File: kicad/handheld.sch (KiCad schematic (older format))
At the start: 23 parts, among them J1 Conn_01x08, J2 61300311121, J3 AVR-PDI-6, SW1 HOLD, SW2 PAUSE, SW3 SDROP, SW4 HDROP, SW5 ROTR, SW6 RIGHT, SW7 ROTL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

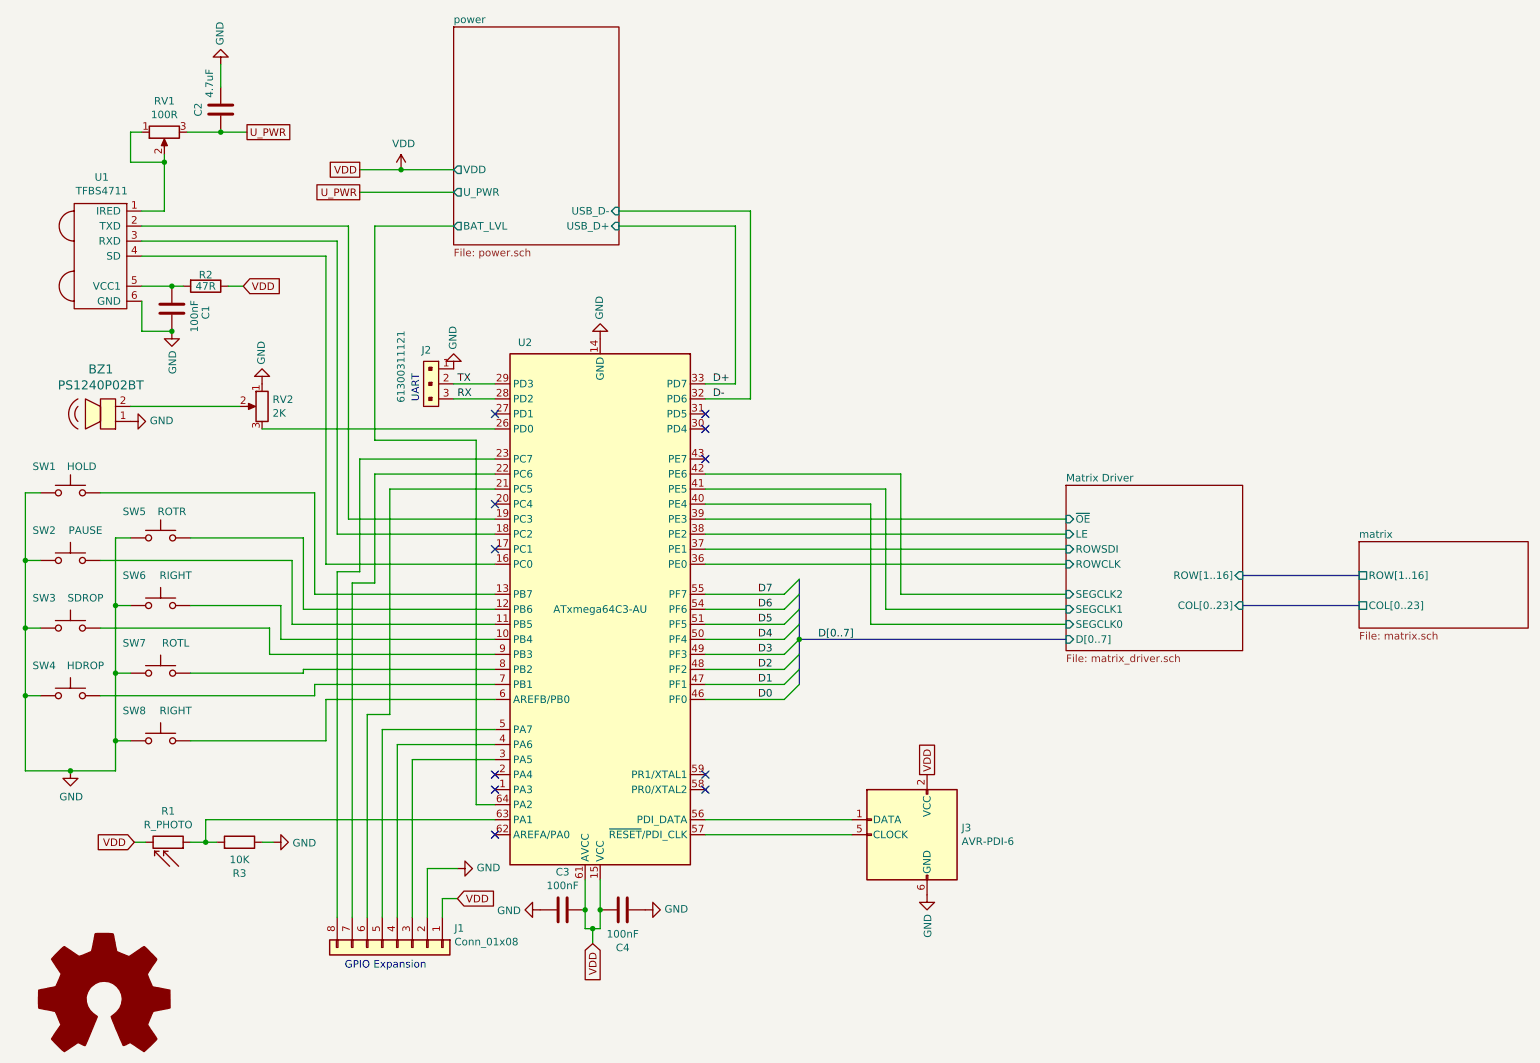
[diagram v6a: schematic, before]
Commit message: Added power plane and reassigned pinout
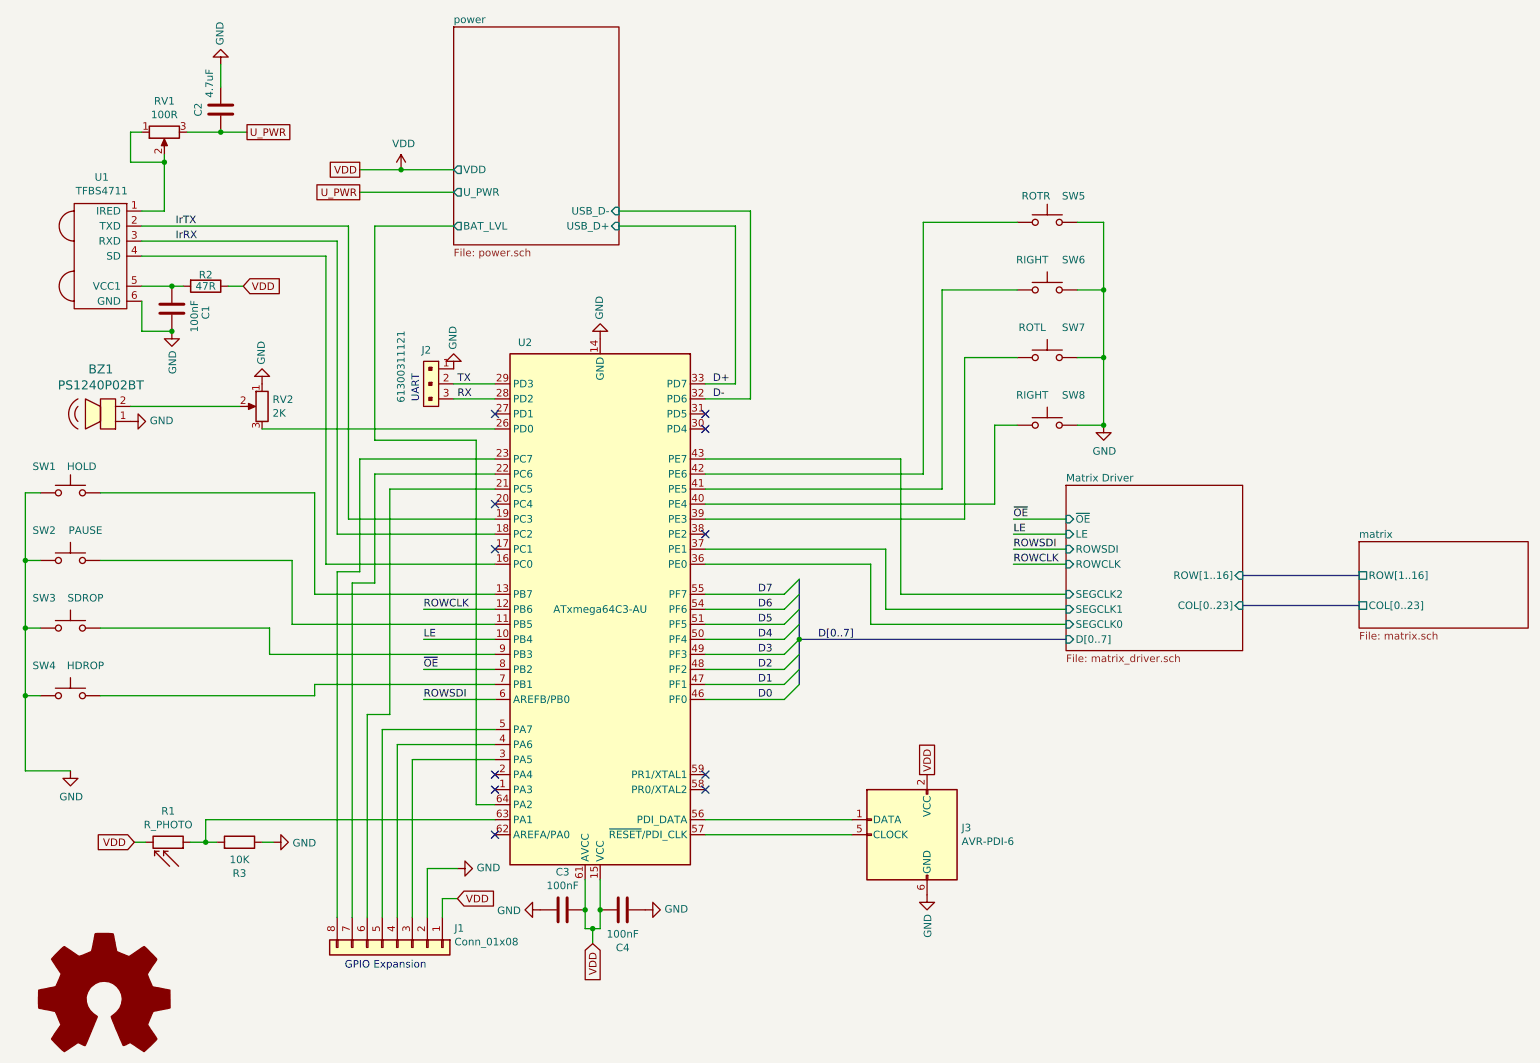
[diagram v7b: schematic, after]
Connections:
- net Matrix Driver/ROWCLK is gone; now on net Matrix Driver/SEGCLK0: U2.36 (PE0)
- net Matrix Driver/ROWSDI is gone; now on net Matrix Driver/SEGCLK1: U2.37 (PE1)
- net Matrix Driver/~OE is gone; now on an unnamed net: U2.39 (PE3)
- net Matrix Driver/SEGCLK0: no longer U2.40 (PE4)
- net Matrix Driver/SEGCLK1: no longer U2.41 (PE5)
- net Matrix Driver/SEGCLK2: now also U2.43 (PE7); no longer U2.42 (PE6)
- net at SW8.2: now also U2.40 (PE4); no longer U2.6 (AREFB/PB0)
- net at SW7.2: no longer U2.8 (PB2)
- net at SW6.2: now also U2.41 (PE5); no longer U2.10 (PB4)
- net at SW5.2: now also U2.42 (PE6); no longer U2.12 (PB6)
- net IrRX: now reaches U1.3 (RXD), U2.18 (PC2)
- net IrTX: now reaches U1.2 (TXD), U2.19 (PC3)
- net Matrix Driver/LE: no longer names the net of U2.38 (PE2)
- new net LE: U2.10 (PB4)
- new net ROWCLK: U2.12 (PB6)
- new net ROWSDI: U2.6 (AREFB/PB0)
- new net ~OE: U2.8 (PB2)
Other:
- moved on the sheet: SW5, SW6, SW7, SW8
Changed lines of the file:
@@
 TX
 Wire Wire Line
-	7550 4375 5150 4375
-Wire Wire Line
-	5150 4275 7550 4275
-Wire Wire Line
-	7550 4175 5150 4175
-Wire Wire Line
-	5150 4075 7550 4075
-Wire Wire Line
 	7550 4775 6250 4775
 Wire Wire Line
-	6250 4775 6250 3975
-Wire Wire Line
-	6250 3975 5150 3975
-Wire Wire Line
 	7550 4675 6350 4675
 Wire Wire Line
-	6350 4675 6350 3875
-Wire Wire Line
-	6350 3875 5150 3875
-Wire Wire Line
 	7550 4575 6450 4575
-Wire Wire Line
-	6450 4575 6450 3775
-Wire Wire Line
-	6450 3775 5150 3775
 $Comp
 L local:TFBS4711 U1
@@
 NoConn ~ 5150 3375
 NoConn ~ 5150 3475
-NoConn ~ 5150 3675
 NoConn ~ 3750 3975
 NoConn ~ 3750 4275
@@
 	1    0    0    -1
 $EndComp
-Connection ~ 925  5750
-Wire Wire Line
-	925  5750 1225 5750
-Wire Wire Line
-	1325 5550 1225 5550
-Connection ~ 1225 5550
-Wire Wire Line
-	1225 5550 1225 5750
-Wire Wire Line
-	2625 5550 2625 5275
-Wire Wire Line
-	2625 5275 3750 5275
-Wire Wire Line
-	2625 5550 1725 5550
+Wire Wire Line
+	3275 5275 3750 5275
 Wire Wire Line
 	2550 5250 2550 5175
@@
 	2550 5175 3750 5175
 Wire Wire Line
-	2475 5100 2475 5075
-Wire Wire Line
-	2475 5075 3750 5075
+	3275 5075 3750 5075
 Wire Wire Line
 	2250 4800 2250 4975
@@
 	2550 4575 3750 4575
 Wire Wire Line
-	2475 4200 2475 4675
-Wire Wire Line
-	2475 4675 3750 4675
+	3275 4675 3750 4675
 Wire Wire Line
 	2400 4350 2400 4775
@@
 	2400 4775 3750 4775
 Wire Wire Line
-	2325 4650 2325 4875
-Wire Wire Line
-	2325 4875 3750 4875
+	3275 4875 3750 4875
 $Comp
 L Switch:SW_Push SW4
@@
 Wire Wire Line
 	625  3900 625  4350
-Wire Wire Line
-	1225 4200 1225 4650
 $Comp
 L Switch:SW_Push SW8
 U 1 1 5FC41930
-P 1525 5550
-F 0 "SW8" H 1350 5750 50  0000 C CNN
-F 1 "RIGHT" H 1625 5750 50  0000 C CNN
-F 2 "Button_Switch_THT:SW_PUSH-12mm" H 1525 5750 50  0001 C CNN
-F 3 "~" H 1525 5750 50  0001 C CNN
-	1    1525 5550
-	1    0    0    -1
+P 7425 3450
+F 0 "SW8" H 7250 3650 50  0000 C CNN
+F 1 "RIGHT" H 7525 3650 50  0000 C CNN
+F 2 "Button_Switch_THT:SW_PUSH-12mm" H 7425 3650 50  0001 C CNN
+F 3 "~" H 7425 3650 50  0001 C CNN
+	1    7425 3450
+	-1   0    0    -1
 $EndComp
 $Comp
 L Switch:SW_Push SW7
 U 1 1 5FC4193A
-P 1525 5100
-F 0 "SW7" H 1350 5300 50  0000 C CNN
-F 1 "ROTL" H 1625 5300 50  0000 C CNN
-F 2 "Button_Switch_THT:SW_PUSH-12mm" H 1525 5300 50  0001 C CNN
-F 3 "~" H 1525 5300 50  0001 C CNN
-	1    1525 5100
-	1    0    0    -1
+P 7425 3000
+F 0 "SW7" H 7250 3200 50  0000 C CNN
+F 1 "ROTL" H 7525 3200 50  0000 C CNN
+F 2 "Button_Switch_THT:SW_PUSH-12mm" H 7425 3200 50  0001 C CNN
+F 3 "~" H 7425 3200 50  0001 C CNN
+	1    7425 3000
+	-1   0    0    -1
 $EndComp
 $Comp
 L Switch:SW_Push SW6
 U 1 1 5FC41944
-P 1525 4650
-F 0 "SW6" H 1350 4850 50  0000 C CNN
-F 1 "RIGHT" H 1625 4850 50  0000 C CNN
-F 2 "Button_Switch_THT:SW_PUSH-12mm" H 1525 4850 50  0001 C CNN
-F 3 "~" H 1525 4850 50  0001 C CNN
-	1    1525 4650
-	1    0    0    -1
+P 7425 2550
+F 0 "SW6" H 7250 2750 50  0000 C CNN
+F 1 "RIGHT" H 7525 2750 50  0000 C CNN
+F 2 "Button_Switch_THT:SW_PUSH-12mm" H 7425 2750 50  0001 C CNN
+F 3 "~" H 7425 2750 50  0001 C CNN
+	1    7425 2550
+	-1   0    0    -1
 $EndComp
 $Comp
 L Switch:SW_Push SW5
 U 1 1 5FC4194E
-P 1525 4200
-F 0 "SW5" H 1350 4375 50  0000 C CNN
-F 1 "ROTR" H 1600 4375 50  0000 C CNN
-F 2 "Button_Switch_THT:SW_PUSH-12mm" H 1525 4400 50  0001 C CNN
-F 3 "~" H 1525 4400 50  0001 C CNN
-	1    1525 4200
-	1    0    0    -1
-$EndComp
-Wire Wire Line
-	1725 5100 2475 5100
+P 7425 2100
+F 0 "SW5" H 7250 2275 50  0000 C CNN
+F 1 "ROTR" H 7500 2275 50  0000 C CNN
+F 2 "Button_Switch_THT:SW_PUSH-12mm" H 7425 2300 50  0001 C CNN
+F 3 "~" H 7425 2300 50  0001 C CNN
+	1    7425 2100
+	-1   0    0    -1
+$EndComp
 Wire Wire Line
 	1125 4800 2250 4800
-Wire Wire Line
-	1725 4650 2325 4650
-Wire Wire Line
-	1325 4650 1225 4650
-Connection ~ 1225 4650
-Wire Wire Line
-	1225 4650 1225 5100
-Wire Wire Line
-	1325 5100 1225 5100
-Connection ~ 1225 5100
-Wire Wire Line
-	1225 5100 1225 5550
 Wire Wire Line
 	725  4800 625  4800
@@
 	1125 4350 2400 4350
 Wire Wire Line
-	2475 4200 1725 4200
-Wire Wire Line
-	1325 4200 1225 4200
+	6250 4775 6250 4375
+Wire Wire Line
+	6250 4375 5150 4375
+Wire Wire Line
+	6350 4675 6350 4275
+Wire Wire Line
+	6350 4275 5150 4275
+Wire Wire Line
+	6450 4575 6450 3675
+Wire Wire Line
+	6450 3675 5150 3675
+Wire Wire Line
+	7225 2100 6600 2100
+Wire Wire Line
+	6600 2100 6600 3775
+Wire Wire Line
+	7225 2550 6725 2550
+Wire Wire Line
+	6725 2550 6725 3875
+Wire Wire Line
+	5150 3775 6600 3775
+Wire Wire Line
+	5150 3875 6725 3875
+Wire Wire Line
+	7225 3450 7075 3450
+Wire Wire Line
+	7075 3450 7075 3975
+Wire Wire Line
+	7075 3975 5150 3975
+Wire Wire Line
+	7225 3000 6875 3000
+Wire Wire Line
+	6875 3000 6875 4075
+Wire Wire Line
+	6875 4075 5150 4075
+Wire Wire Line
+	7625 3450 7800 3450
+Wire Wire Line
+	7800 3450 7800 3000
+Wire Wire Line
+	7800 2100 7625 2100
+Wire Wire Line
+	7625 2550 7800 2550
+Connection ~ 7800 2550
+Wire Wire Line
+	7800 2550 7800 2100
+Wire Wire Line
+	7625 3000 7800 3000
+Connection ~ 7800 3000
+Wire Wire Line
+	7800 3000 7800 2550
+$Comp
+L power:GND #PWR0101
+U 1 1 5FC72BB8
+P 7800 3450
+F 0 "#PWR0101" H 7800 3200 50  0001 C CNN
+F 1 "GND" H 7805 3277 50  0000 C CNN
+F 2 "" H 7800 3450 50  0001 C CNN
+F 3 "" H 7800 3450 50  0001 C CNN
+	1    7800 3450
+	1    0    0    -1
+$EndComp
+Connection ~ 7800 3450
+NoConn ~ 5150 4175
+Text Label 3275 5275 0    50   ~ 0
+ROWSDI
+Wire Wire Line
+	7550 4275 7200 4275
+Text Label 7200 4275 0    50   ~ 0
+ROWSDI
+Wire Wire Line
+	7550 4375 7200 4375
+Text Label 7200 4375 0    50   ~ 0
+ROWCLK
+Text Label 7200 4175 0    50   ~ 0
+LE
+Wire Wire Line
+	7200 4175 7550 4175
+Text Label 7200 4075 0    50   ~ 0
+~OE
+Wire Wire Line
+	7200 4075 7550 4075
+Text Label 3275 5075 0    50   ~ 0
+~OE
+Text Label 3275 4875 0    50   ~ 0
+LE
+Text Label 3275 4675 0    50   ~ 0
+ROWCLK
 Wire Bus Line
 	5775 4875 5775 5175
 Wire Bus Line
 	5775 4475 5775 4875
+Text Label 1625 2125 0    50   ~ 0
+IrTX
+Text Label 1625 2225 0    50   ~ 0
+IrRX
 $EndSCHEMATC

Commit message: Wired up buzzer and LDR
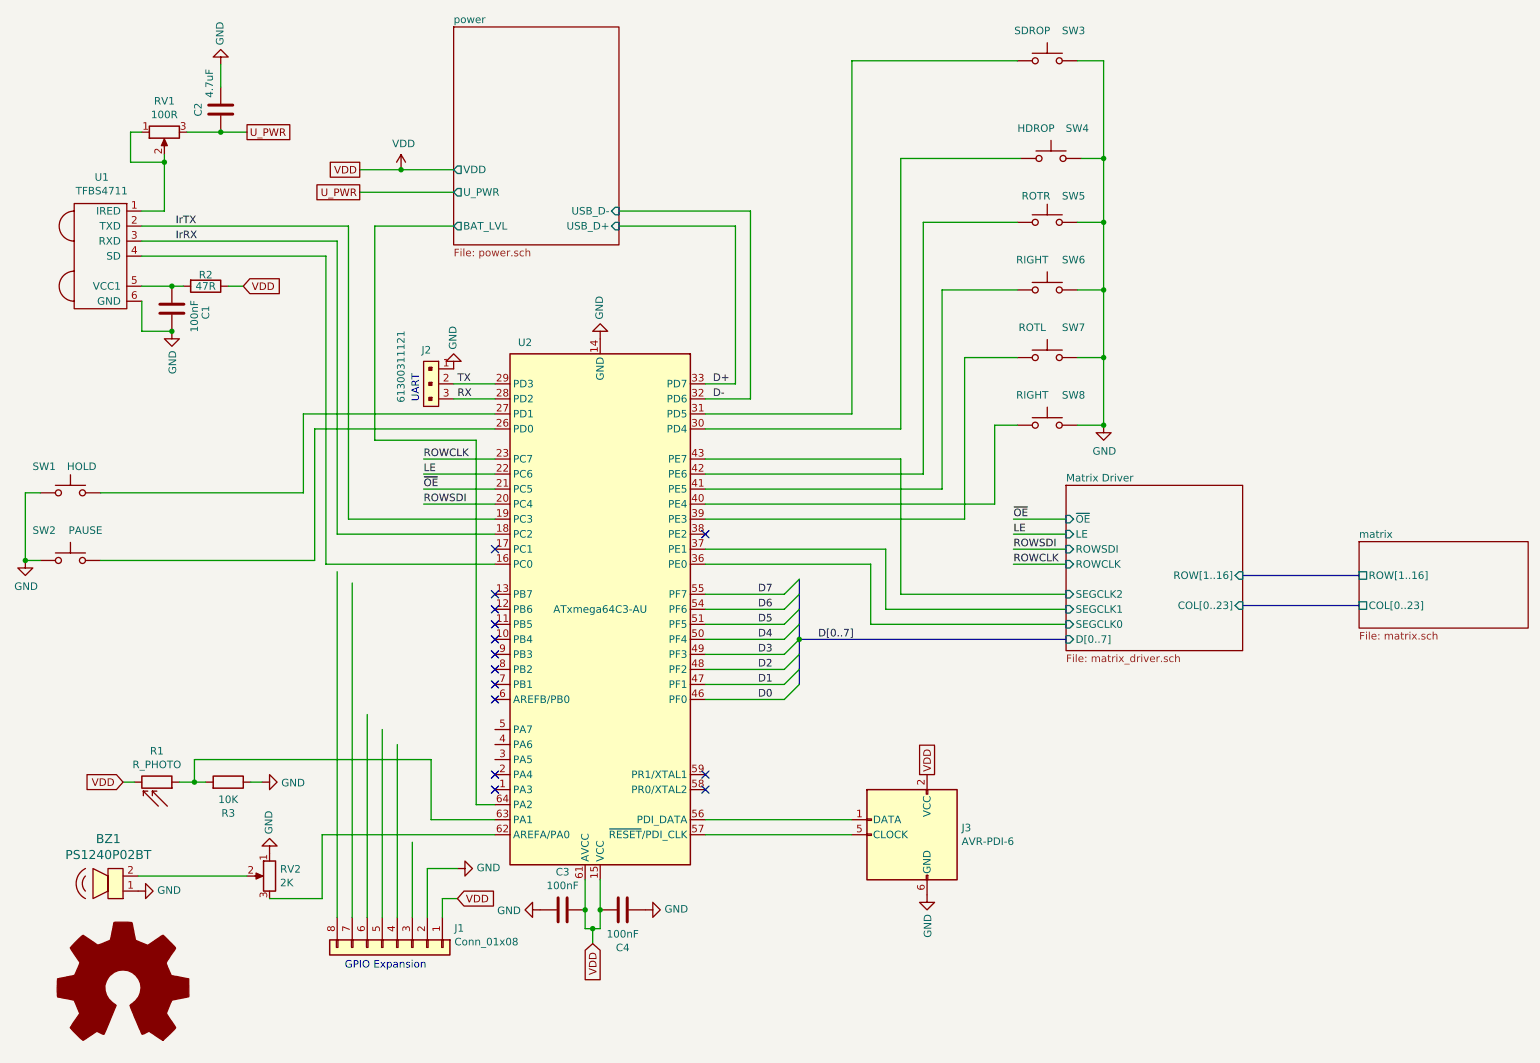
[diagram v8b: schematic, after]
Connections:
- wire segments 143 -> 133
- no-connect marks 11 -> 14
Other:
- moved on the sheet: BZ1, R1, R3, RV2, SW3, SW4
